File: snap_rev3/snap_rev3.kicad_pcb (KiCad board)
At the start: 2 copper layers, 60 x 22 mm, 30 parts, among them J1 SJ2-35863B1, P1 CONN_02X05, Q1 TSM2301, SW1 TL3304AF260QJ, U1 TPS610986, U2 MDBT42Q, Y1 32786Hz

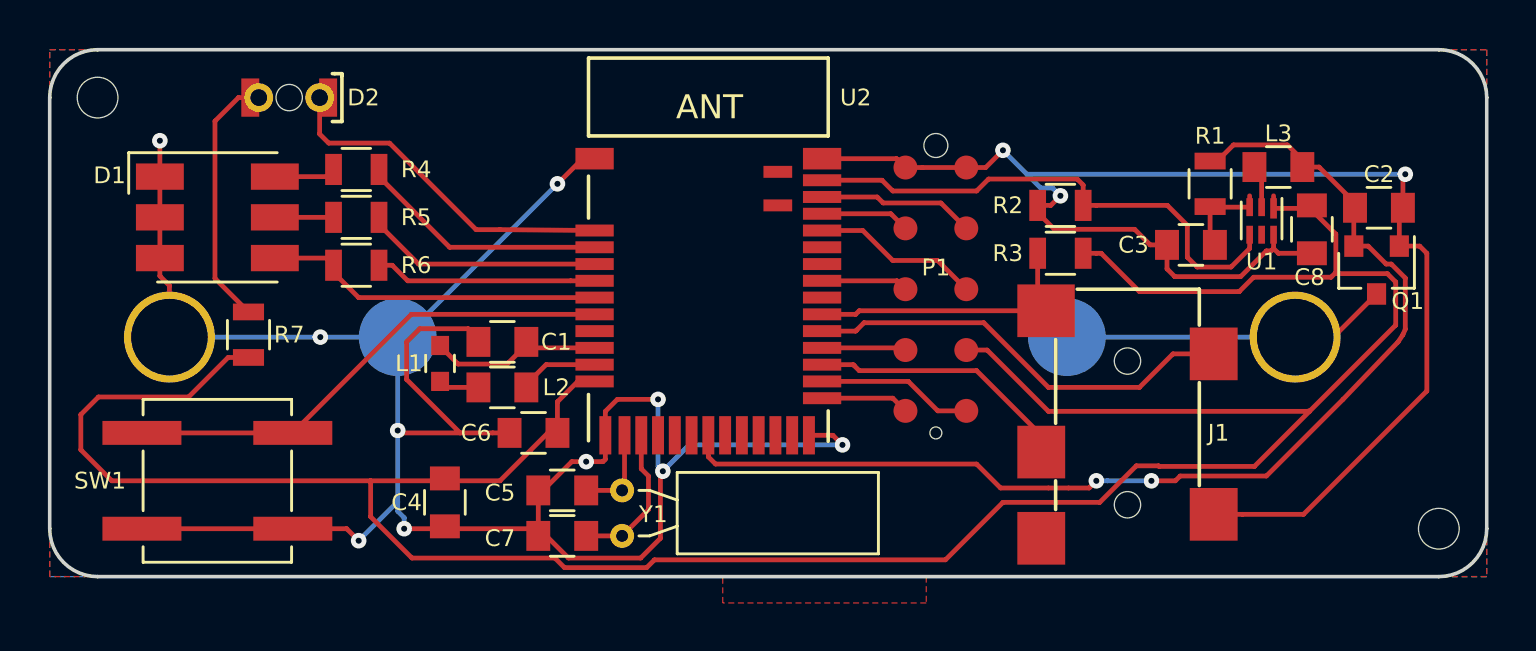
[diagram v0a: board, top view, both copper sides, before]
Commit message: Updated PCB with updated programming connector
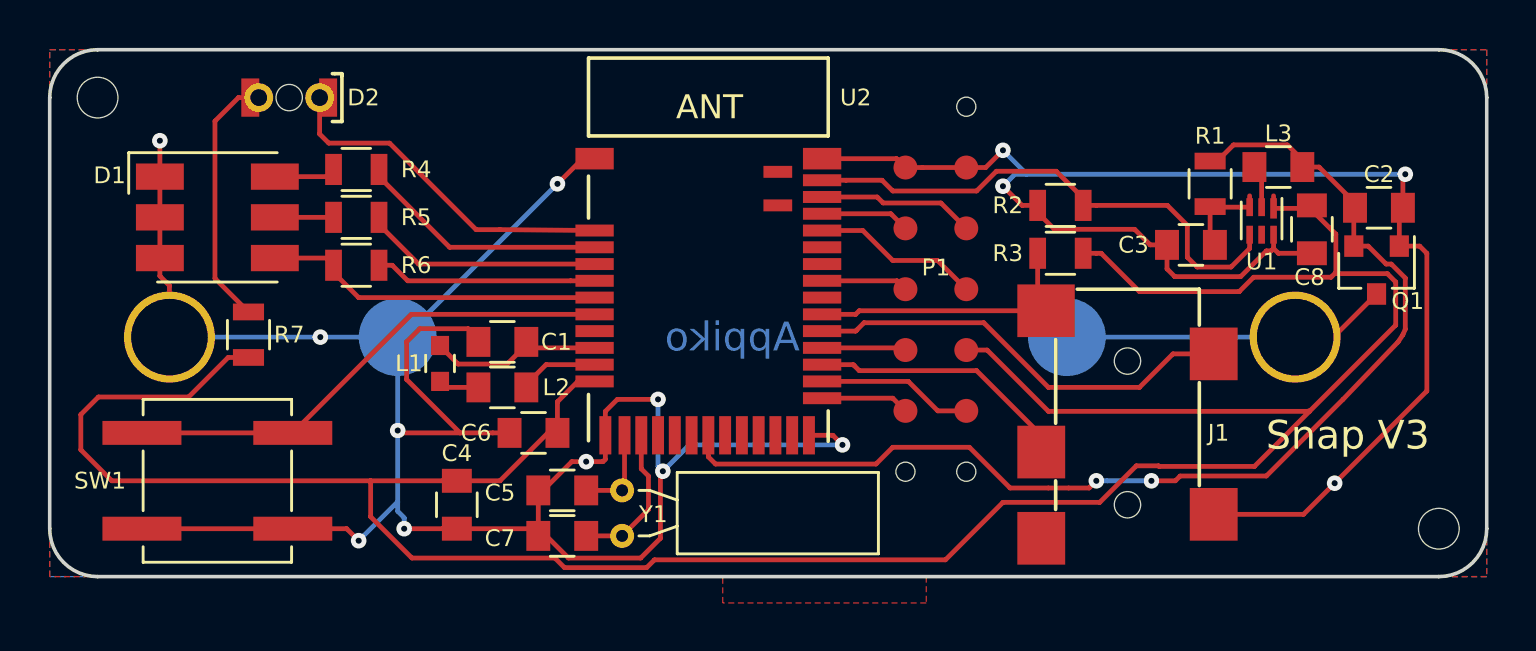
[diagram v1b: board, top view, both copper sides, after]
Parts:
- moved C4 0.51 mm to (67.0, 107.0)
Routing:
- net /VBAT: track 47.6 -> 48.2 mm
- net GND: track 162.5 -> 162.6 mm, vias 13 -> 14
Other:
- board text added: "Appiko"
- board text added: "Snap V3"
